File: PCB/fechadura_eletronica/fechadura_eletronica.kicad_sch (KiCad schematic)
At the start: 12 parts, among them J1 Relay Module, J2 RFID - RC522, J3 LCD 16X2, J4 DY50, SW1 reset button, U1 LM7805 - regulator, U2 ESP32-DEVKIT-V1

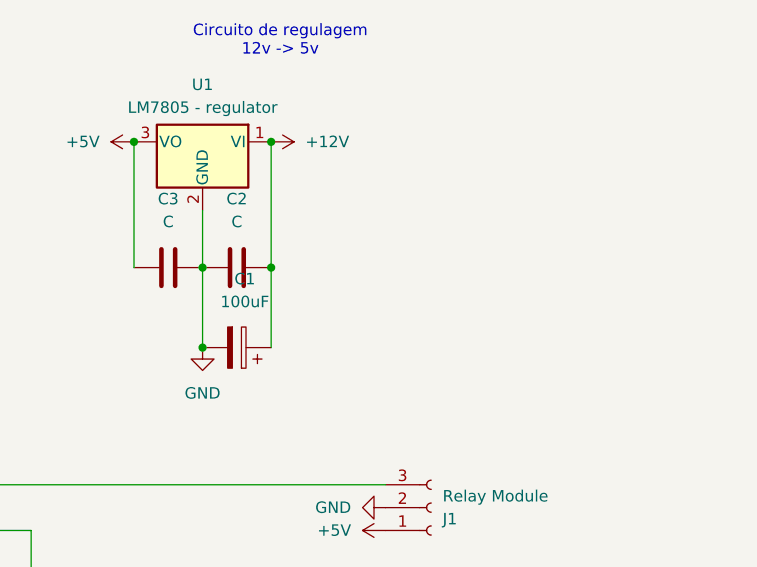
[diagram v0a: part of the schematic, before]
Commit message: adicionado regulador 3.3v LD1117 e PCB refatorada
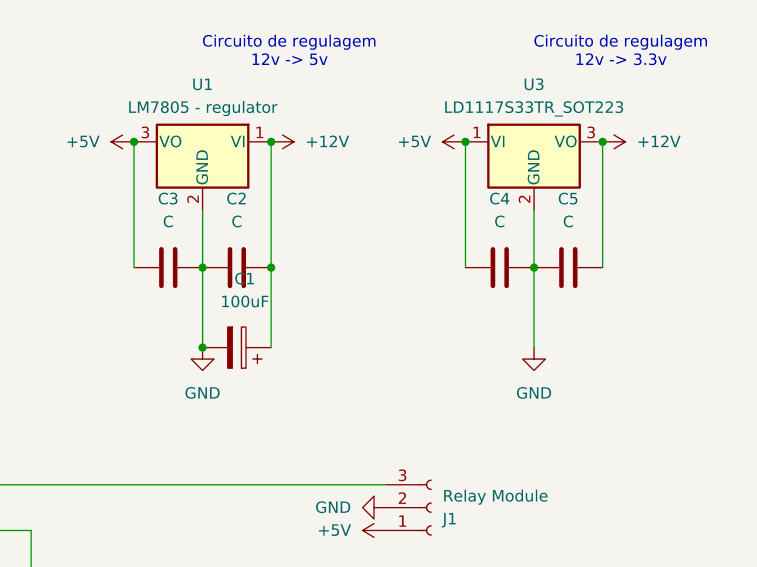
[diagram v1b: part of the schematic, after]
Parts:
- added C4, C5: C, Capacitor_THT:C_Radial_D6.3mm_H7.0mm_P2.50mm, symbol Device:C
- added U3: LD1117S33TR_SOT223, Package_TO_SOT_THT:TO-220-3_Vertical, symbol Regulator_Linear:LM7805_TO220
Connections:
- net +12V: now also C5.2, U3.3 (VO)
- net +5V: now also C4.1, U3.1 (VI)
- net GND: now also C4.2, C5.1, U3.2 (GND)
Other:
- note added: "Circuito de regulagem 12v -> 3.3v"

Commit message: versao final
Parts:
- added J5: Screw_Terminal_01x02, TerminalBlock_MetzConnect:TerminalBlock_MetzConnect_Type094_RT03502HBLU_1x02_P5.00mm_Horizontal, symbol Connector:Screw_Terminal_01x02
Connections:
- net +12V: now also J5.1 (Pin_1)
- net GND: now also J5.2 (Pin_2)
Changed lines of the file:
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@@
+	)
+	(symbol
+		(lib_id "Connector:Screw_Terminal_01x02")
+		(at 212.09 113.03 0)
+		(unit 1)
+		(exclude_from_sim no)
+		(in_bom yes)
+		(on_board yes)
+		(dnp no)
+		(fields_autoplaced yes)
+		(property "Reference" "J5"
+			(at 214.63 113.0299 0)
+			(effects
+				(font
+					(size 1.27 1.27)
+				)
+				(justify left)
+			)
+		)
+		(property "Value" "Screw_Terminal_01x02"
+			(at 214.63 115.5699 0)
+			(effects
+				(font
+					(size 1.27 1.27)
+				)
+				(justify left)
+			)
+		)
+		(property "Footprint" "TerminalBlock_MetzConnect:TerminalBlock_MetzConnect_Type094_RT03502HBLU_1x02_P5.00mm_Horizontal"
+			(at 212.09 113.03 0)
+			(effects
+				(font
+					(size 1.27 1.27)
+				)
+				(hide yes)
+			)
+		)
+		(property "Datasheet" "~"
+			(at 212.09 113.03 0)
+			(effects
+				(font
+					(size 1.27 1.27)
+				)
+				(hide yes)
+			)
+		)
+		(property "Description" "Generic screw terminal, single row, 01x02, script generated (kicad-library-utils/schlib/autogen/connector/)"
+			(at 212.09 113.03 0)
+			(effects
+				(font
+					(size 1.27 1.27)
+				)
+				(hide yes)
+			)
+		)
+		(pin "1"
+		)
+		(pin "2"
+		)
+		(instances
+			(project "fechadura_eletronica"
+				(path "/713915d2-744a-4423-8dcc-c9aa1cefff80"
+					(reference "J5")
+					(unit 1)
+				)
+			)
+		)
 	)
 	(symbol
@@
 	(symbol
 		(lib_id "power:GND")
+		(at 207.01 115.57 270)
+		(unit 1)
+		(exclude_from_sim no)
+		(in_bom yes)
+		(on_board yes)
+		(dnp no)
+		(fields_autoplaced yes)
+		(property "Reference" "#PWR022"
+			(at 200.66 115.57 0)
+			(effects
+				(font
+					(size 1.27 1.27)
+				)
+				(hide yes)
+			)
+		)
+		(property "Value" "GND"
+			(at 203.2 115.5699 90)
+			(effects
+				(font
+					(size 1.27 1.27)
+				)
+				(justify right)
+			)
+		)
+		(property "Footprint" ""
+			(at 207.01 115.57 0)
+			(effects
+				(font
+					(size 1.27 1.27)
+				)
+				(hide yes)
+			)
+		)
+		(property "Datasheet" ""
+			(at 207.01 115.57 0)
+			(effects
+				(font
+					(size 1.27 1.27)
+				)
+				(hide yes)
+			)
+		)
+		(property "Description" "Power symbol creates a global label with name \"GND\" , ground"
+			(at 207.01 115.57 0)
+			(effects
+				(font
+					(size 1.27 1.27)
+				)
+				(hide yes)
+			)
+		)
+		(pin "1"
+		)
+		(instances
+			(project "fechadura_eletronica"
+				(path "/713915d2-744a-4423-8dcc-c9aa1cefff80"
+					(reference "#PWR022")
+					(unit 1)
+				)
+			)
+		)
+	)
+	(symbol
+		(lib_id "power:GND")
 		(at 137.16 139.7 180)
 		(unit 1)
@@
 					(unit 1)
 				)
+			)
+		)
+	)
+	(symbol
+		(lib_id "power:+12V")
+		(at 207.01 113.03 90)
+		(unit 1)
+		(exclude_from_sim no)
+		(in_bom yes)
+		(on_board yes)
+		(dnp no)
+		(fields_autoplaced yes)
+		(property "Reference" "#PWR021"
+			(at 210.82 113.03 0)
+			(effects
+				(font
+					(size 1.27 1.27)
+				)
+				(hide yes)
+			)
+		)
+		(property "Value" "+12V"
+			(at 203.2 113.0299 90)
+			(effects
+				(font
+					(size 1.27 1.27)
+				)
+				(justify left)
+			)
+		)
+		(property "Footprint" ""
+			(at 207.01 113.03 0)
+			(effects
+				(font
+					(size 1.27 1.27)
+				)
+				(hide yes)
+			)
+		)
+		(property "Datasheet" ""
+			(at 207.01 113.03 0)
+			(effects
+				(font
+					(size 1.27 1.27)
+				)
+				(hide yes)
+			)
+		)
+		(property "Description" "Power symbol creates a global label with name \"+12V\""
+			(at 207.01 113.03 0)
+			(effects
+				(font
+					(size 1.27 1.27)
+				)
+				(hide yes)
+			)
+		)
+		(pin "1"
+		)
+		(instances
+			(project "fechadura_eletronica"
+				(path "/713915d2-744a-4423-8dcc-c9aa1cefff80"
+					(reference "#PWR021")
+					(unit 1)
+				)
